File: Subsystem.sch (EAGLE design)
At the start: 16 parts

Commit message: Schematic V1
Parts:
- removed U$3: 6PIN-PLUG, Brendan:6PIN-PLUG
- added C1: 22uF, Brendan:CAP0805
- added ESP_PROG, RS232: 4PIN-PLUG, Brendan:4PIN-PLUG
- added POWER_MODULE: 6PIN-PLUG, Brendan:6PIN-PLUG
- added U1: (no value), Brendan:V_REG_LM1117SOT223
- renumbered U$2 to PIXHAWK_COMMS
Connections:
- removed net N$1: U$1.GND@1
- removed net N$2: U$1.9/PWM/AIN/TX2
- removed net N$3: U$1.8/PWM/AIN/RX2
- removed net N$5: U$1.VIN/MAX15V
- removed net N$6: U$1.24/USBDM
- removed net N$7: U$1.25/PWM/RX1
- removed net RX: PIXHAWK_COMMS.P$6
- removed net RXD: X1.RXD
- removed net TX: PIXHAWK_COMMS.P$7
- removed net TXD: X1.TXD
- new net MCUR: POWER_MODULE.P$4, U$1.6/AIN/SCK1
- new net MVOL: POWER_MODULE.P$3, U$1.7/AIN/SS1
- new net RX1: PIXHAWK_COMMS.P$6, U$1.25/PWM/RX1
- new net RX2: ESP_PROG.P$2, U$1.8/PWM/AIN/RX2, X1.TXD
- new net RX3: RS232.P$3, U$1.0/RX3/SDA2
- new net TX1: PIXHAWK_COMMS.P$7, U$1.26/PWM/TX1
- new net TX2: ESP_PROG.P$3, U$1.9/PWM/AIN/TX2, X1.RXD
- new net TX3: RS232.P$2, U$1.1/TX3/SCL2
- net 3.3V: now also C1.1, ESP_PROG.P$4, RS232.P$4, U1.OUT
- net 5V: now also POWER_MODULE.P$5, POWER_MODULE.P$6, U$1.VIN/MAX15V, U1.IN; no longer PIXHAWK_COMMS.P$8
- net GND: now also C1.2, ESP_PROG.P$1, POWER_MODULE.P$1, POWER_MODULE.P$2, RS232.P$1, U$1.GND@1, U1.OUT@1

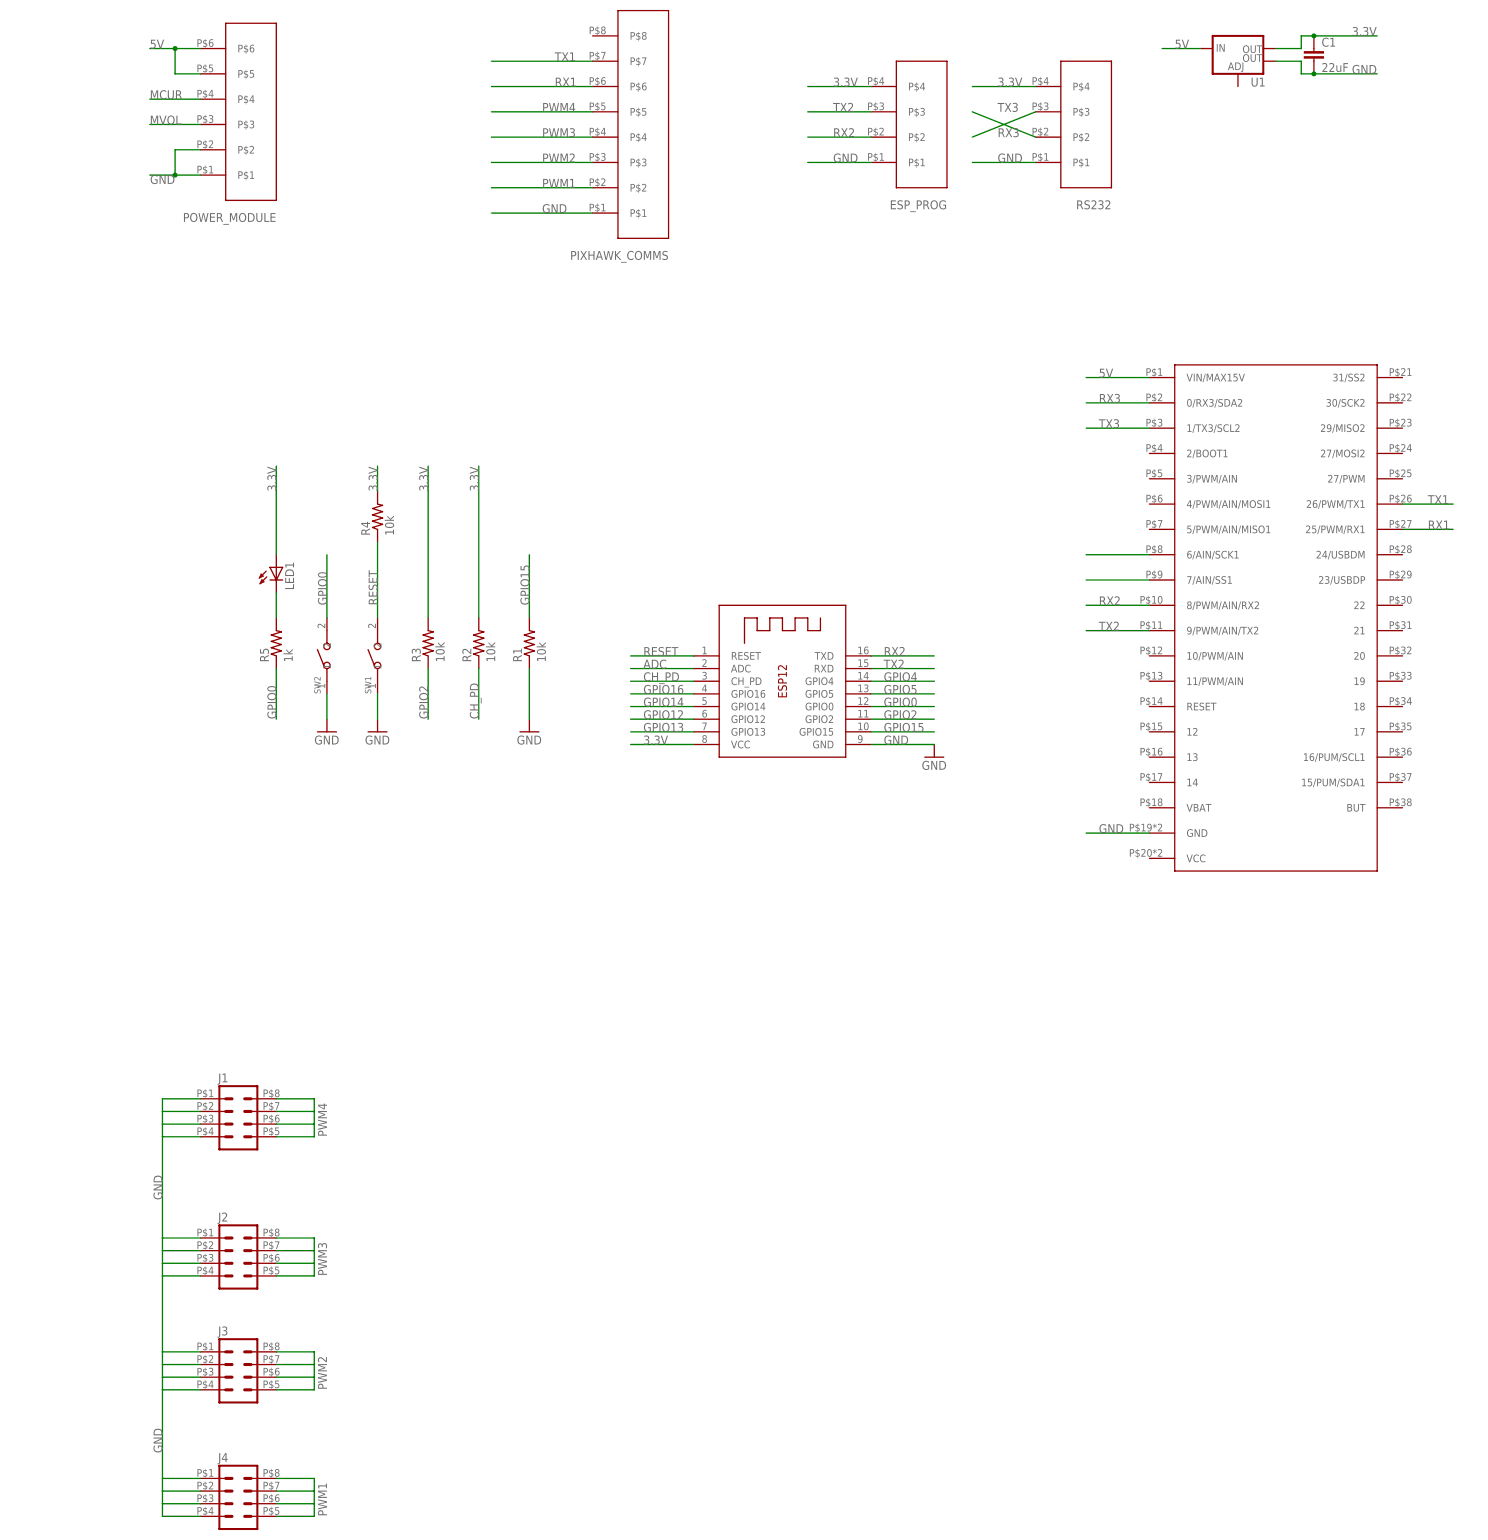
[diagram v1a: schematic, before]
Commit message: Schematic V2\n Check for errors
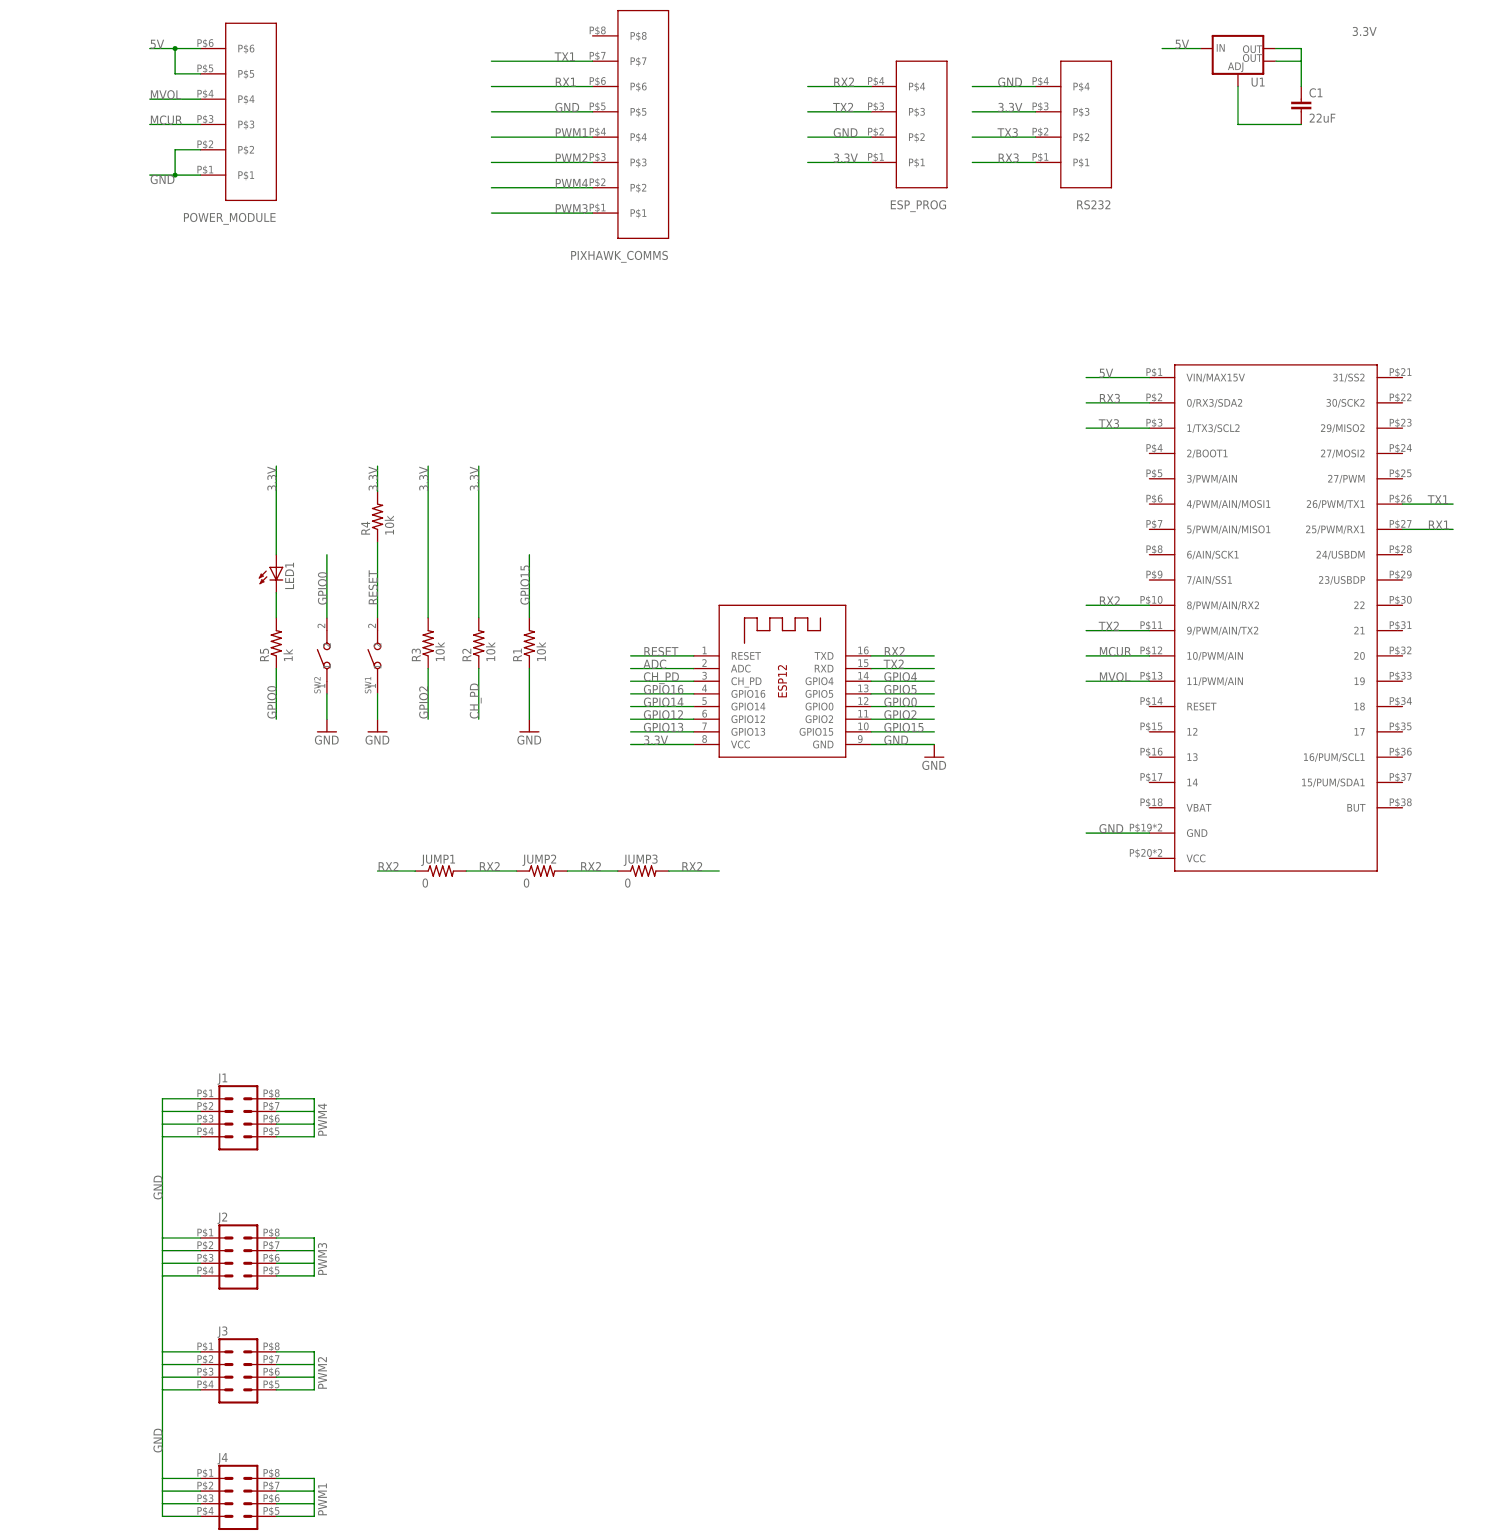
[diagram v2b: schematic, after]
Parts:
- added JUMP1, JUMP2, JUMP3: 0, Brendan:RESISTOR1206
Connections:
- net 3.3V: now also ESP_PROG.P$1, RS232.P$3, U1.OUT@1; no longer ESP_PROG.P$4, RS232.P$4
- net GND: now also ESP_PROG.P$2, PIXHAWK_COMMS.P$5, RS232.P$4, U1.ADJ; no longer ESP_PROG.P$1, PIXHAWK_COMMS.P$1, RS232.P$1, U1.OUT@1
- net MCUR: now also POWER_MODULE.P$3, U$1.10/PWM/AIN; no longer POWER_MODULE.P$4, U$1.6/AIN/SCK1
- net MVOL: now also POWER_MODULE.P$4, U$1.11/PWM/AIN; no longer POWER_MODULE.P$3, U$1.7/AIN/SS1
- net PWM1: now also PIXHAWK_COMMS.P$4; no longer PIXHAWK_COMMS.P$2
- net PWM3: now also PIXHAWK_COMMS.P$1; no longer PIXHAWK_COMMS.P$4
- net PWM4: now also PIXHAWK_COMMS.P$2; no longer PIXHAWK_COMMS.P$5
- net RX2: now also ESP_PROG.P$4, JUMP1.1, JUMP1.2, JUMP2.1, JUMP2.2, JUMP3.1, JUMP3.2; no longer ESP_PROG.P$2
- net RX3: now also RS232.P$1; no longer RS232.P$3
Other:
- moved on the sheet: C1
